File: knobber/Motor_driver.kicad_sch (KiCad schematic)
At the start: 28 parts, among them U601 TMC6300-LA-T, U602 LMV321

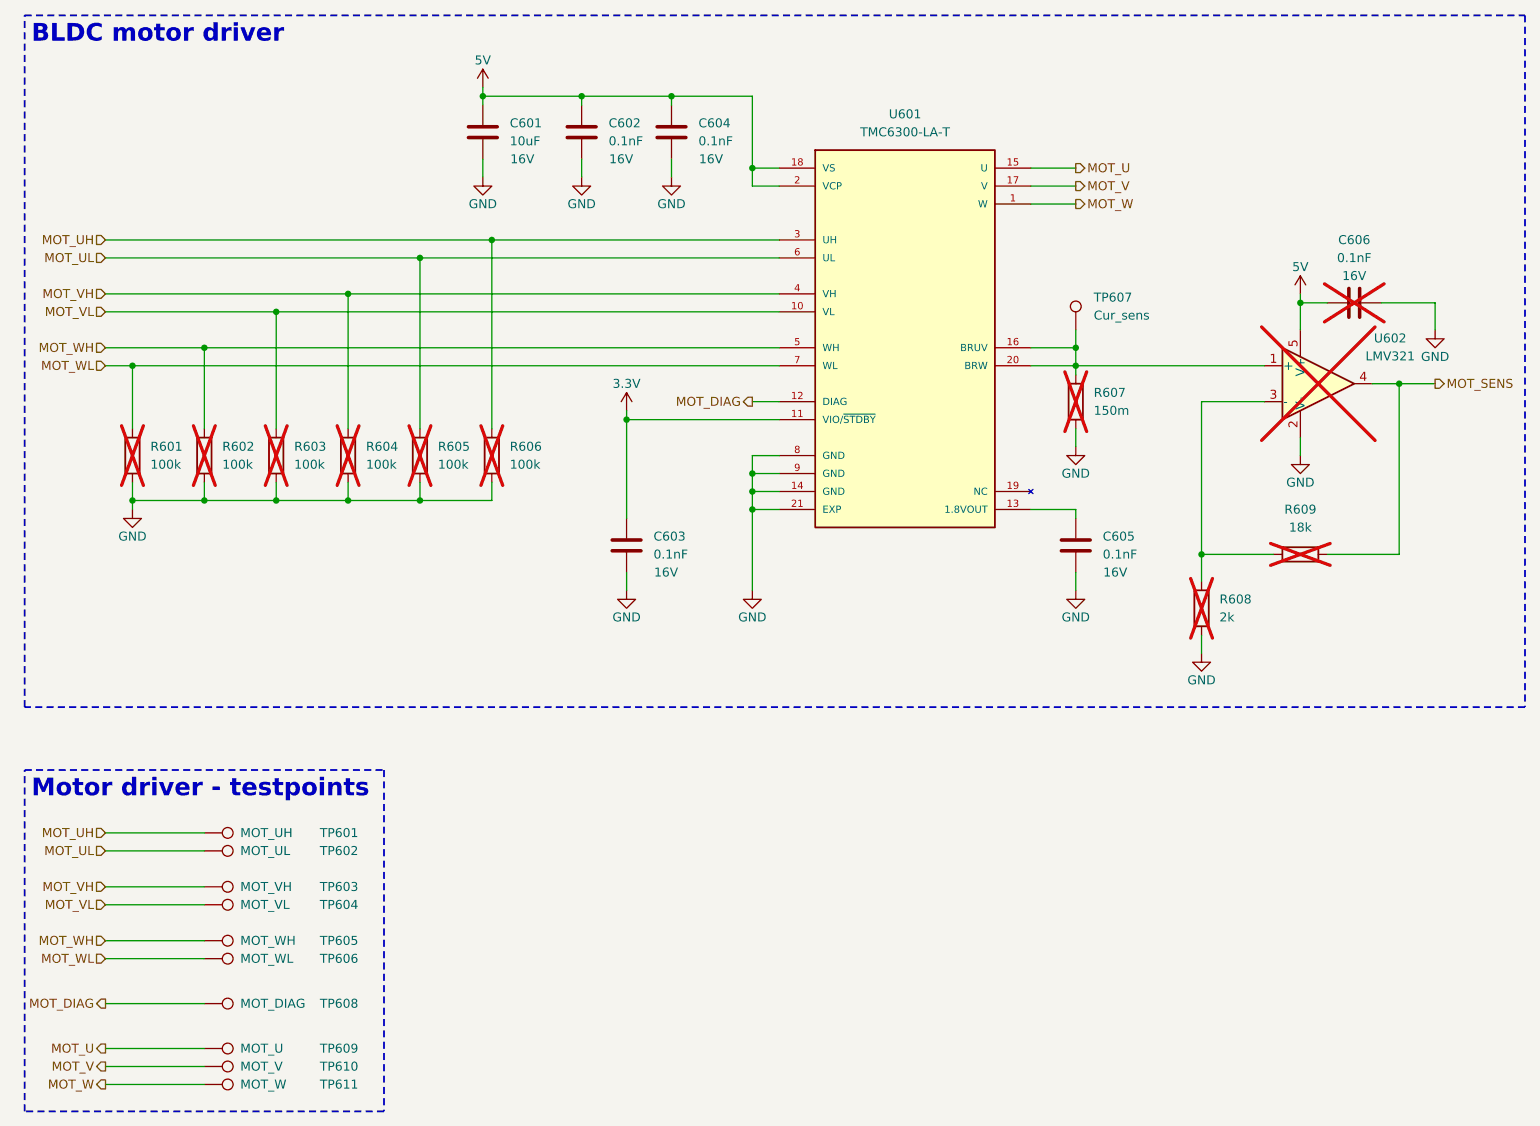
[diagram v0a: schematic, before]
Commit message: Updated schematic and PCB
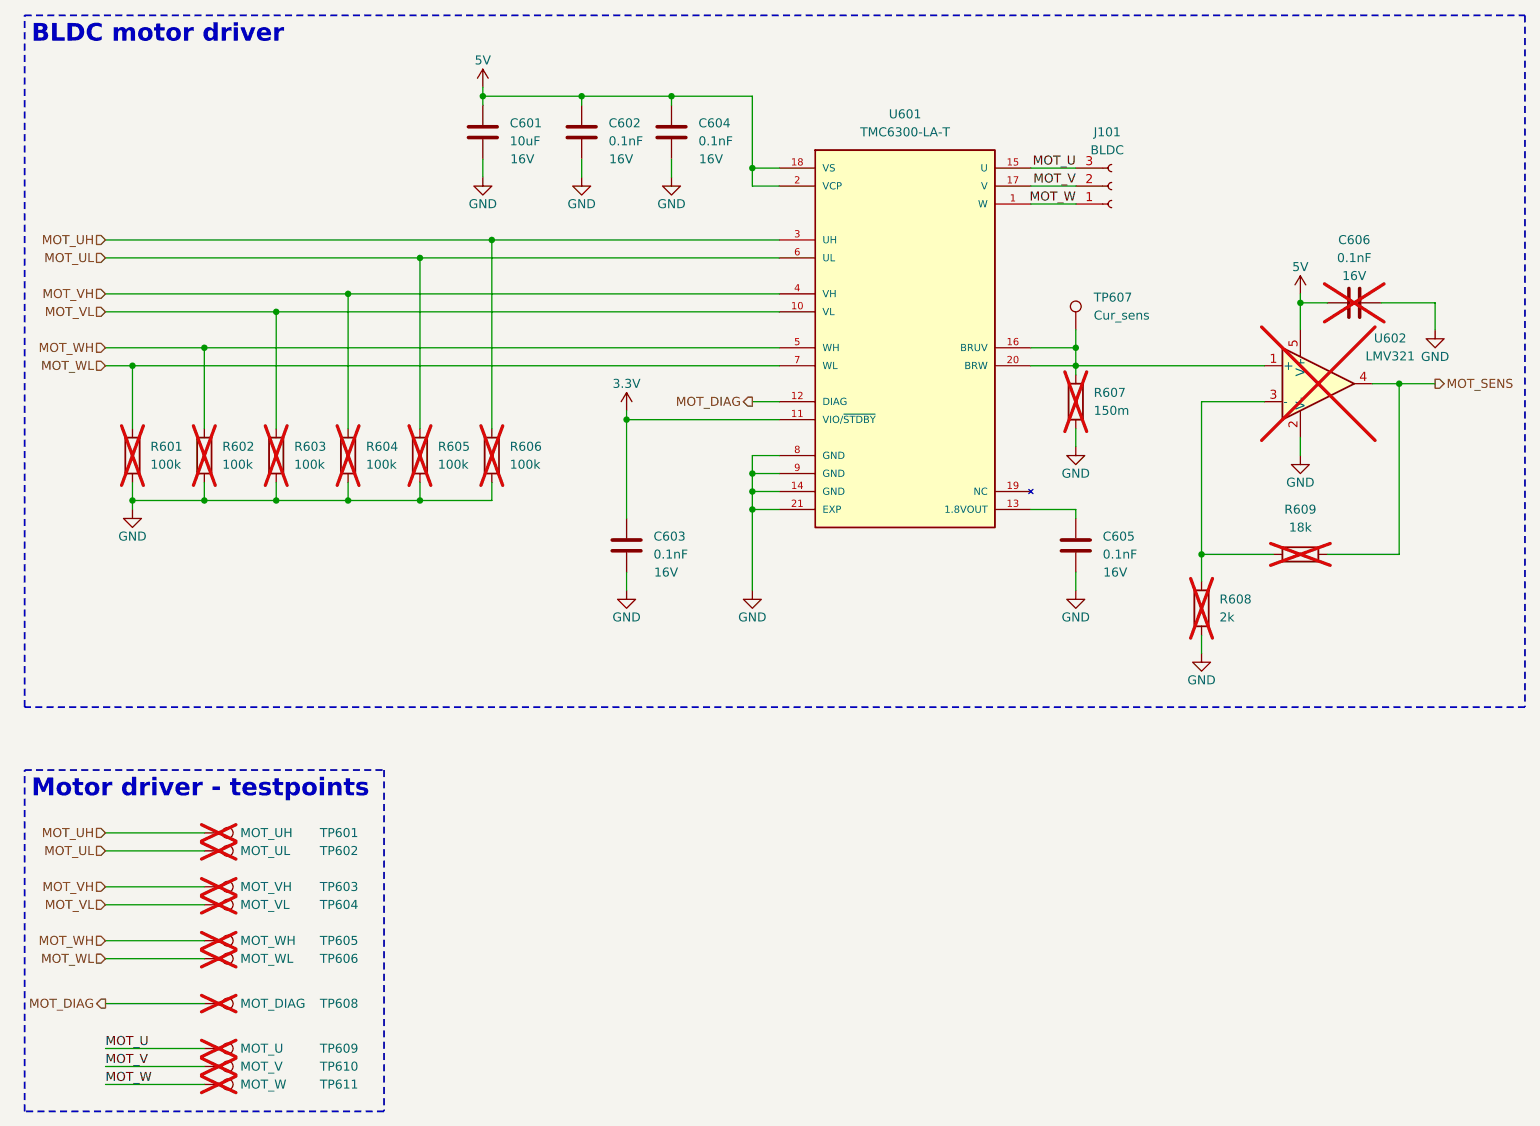
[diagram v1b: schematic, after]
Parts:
- added J101: BLDC, Connector_Molex:Molex_SPOX_5267-03A_1x03_P2.50mm_Vertical, symbol Connector:Conn_01x03_Socket
- TP601, TP602, TP603, TP604, TP605, TP606, TP608, TP609, TP610, TP611: now not fitted; now left out of the parts list
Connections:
- net MOT_U: now also J101.3 (Pin_3)
- net MOT_V: now also J101.2 (Pin_2)
- net MOT_W: now also J101.1 (Pin_1)
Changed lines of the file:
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@@
 		)
 	)
-	(hierarchical_label "MOT_DIAG"
-		(shape output)
-		(at 54.61 162.56 180)
+	(label "MOT_V"
+		(at 54.61 171.45 0)
 		(effects
 			(font
 				(size 1.27 1.27)
 			)
-			(justify right)
+			(justify left bottom)
 		)
 	)
-	(hierarchical_label "MOT_WL"
-		(shape input)
-		(at 54.61 156.21 180)
+	(label "MOT_W"
+		(at 54.61 173.99 0)
 		(effects
 			(font
 				(size 1.27 1.27)
 			)
-			(justify right)
+			(justify left bottom)
 		)
 	)
-	(hierarchical_label "MOT_WH"
-		(shape input)
-		(at 54.61 69.85 180)
+	(label "MOT_V"
+		(at 191.77 46.99 180)
 		(effects
 			(font
 				(size 1.27 1.27)
 			)
-			(justify right)
+			(justify right bottom)
 		)
 	)
-	(hierarchical_label "MOT_W"
-		(shape output)
-		(at 54.61 173.99 180)
+	(label "MOT_U"
+		(at 191.77 44.45 180)
 		(effects
 			(font
 				(size 1.27 1.27)
 			)
-			(justify right)
+			(justify right bottom)
 		)
 	)
-	(hierarchical_label "MOT_W"
-		(shape output)
-		(at 191.77 49.53 0)
+	(label "MOT_W"
+		(at 191.77 49.53 180)
 		(effects
 			(font
 				(size 1.27 1.27)
 			)
-			(justify left)
+			(justify right bottom)
 		)
 	)
-	(hierarchical_label "MOT_U"
-		(shape output)
-		(at 191.77 44.45 0)
+	(label "MOT_U"
+		(at 54.61 168.91 0)
 		(effects
 			(font
 				(size 1.27 1.27)
 			)
-			(justify left)
+			(justify left bottom)
 		)
 	)
-	(hierarchical_label "MOT_V"
+	(hierarchical_label "MOT_DIAG"
 		(shape output)
-		(at 191.77 46.99 0)
+		(at 54.61 162.56 180)
 		(effects
 			(font
 				(size 1.27 1.27)
 			)
-			(justify left)
+			(justify right)
 		)
 	)
-	(hierarchical_label "MOT_U"
-		(shape output)
-		(at 54.61 168.91 180)
+	(hierarchical_label "MOT_WL"
+		(shape input)
+		(at 54.61 156.21 180)
 		(effects
 			(font
@@
 	(hierarchical_label "MOT_WH"
 		(shape input)
-		(at 54.61 153.67 180)
+		(at 54.61 69.85 180)
 		(effects
 			(font
@@
 		)
 	)
-	(hierarchical_label "MOT_UL"
+	(hierarchical_label "MOT_WH"
 		(shape input)
-		(at 54.61 140.97 180)
+		(at 54.61 153.67 180)
 		(effects
 			(font
@@
 		)
 	)
-	(hierarchical_label "MOT_V"
-		(shape output)
-		(at 54.61 171.45 180)
+	(hierarchical_label "MOT_UL"
+		(shape input)
+		(at 54.61 140.97 180)
 		(effects
 			(font
@@
 		(unit 1)
 		(exclude_from_sim no)
-		(in_bom yes)
-		(on_board yes)
-		(dnp no)
+		(in_bom no)
+		(on_board no)
+		(dnp yes)
 		(property "Reference" "TP601"
 			(at 87.63 138.43 90)
@@
 	)
 	(symbol
-		(lib_id "Connector:TestPoint")
-		(at 68.58 146.05 270)
+		(lib_id "Connector:Conn_01x03_Socket")
+		(at 196.85 46.99 0)
 		(mirror x)
 		(unit 1)
@@
 		(on_board yes)
 		(dnp no)
+		(fields_autoplaced yes)
+		(property "Reference" "J101"
+			(at 196.215 39.37 0)
+			(effects
+				(font
+					(size 1.27 1.27)
+				)
+			)
+		)
+		(property "Value" "BLDC"
+			(at 196.215 41.91 0)
+			(effects
+				(font
+					(size 1.27 1.27)
+				)
+			)
+		)
+		(property "Footprint" "Connector_Molex:Molex_SPOX_5267-03A_1x03_P2.50mm_Vertical"
+			(at 196.85 46.99 0)
+			(effects
+				(font
+					(size 1.27 1.27)
+				)
+				(hide yes)
+			)
+		)
+		(property "Datasheet" "~"
+			(at 196.85 46.99 0)
+			(effects
+				(font
+					(size 1.27 1.27)
+				)
+				(hide yes)
+			)
+		)
+		(property "Description" "Generic connector, single row, 01x03, script generated"
+			(at 196.85 46.99 0)
+			(effects
+				(font
+					(size 1.27 1.27)
+				)
+				(hide yes)
+			)
+		)
+		(pin "2"
+		)
+		(pin "1"
+		)
+		(pin "3"
+		)
+		(instances
+			(project "knobber"
+				(path "/09c102b8-dfc1-4666-b1e2-d0c53b401993/09b435d4-5eb0-4cf9-81af-6c2df0af7c36"
+					(reference "J101")
+					(unit 1)
+				)
+			)
+		)
+	)
+	(symbol
+		(lib_id "Connector:TestPoint")
+		(at 68.58 146.05 270)
+		(mirror x)
+		(unit 1)
+		(exclude_from_sim no)
+		(in_bom no)
+		(on_board no)
+		(dnp yes)
 		(property "Reference" "TP603"
 			(at 87.63 146.05 90)
@@
 		(unit 1)
 		(exclude_from_sim no)
-		(in_bom yes)
-		(on_board yes)
-		(dnp no)
+		(in_bom no)
+		(on_board no)
+		(dnp yes)
 		(property "Reference" "TP608"
 			(at 87.63 162.56 90)
@@
 		(unit 1)
 		(exclude_from_sim no)
-		(in_bom yes)
-		(on_board yes)
-		(dnp no)
+		(in_bom no)
+		(on_board no)
+		(dnp yes)
 		(property "Reference" "TP609"
 			(at 87.63 168.91 90)
@@
 		(unit 1)
 		(exclude_from_sim no)
-		(in_bom yes)
-		(on_board yes)
-		(dnp no)
+		(in_bom no)
+		(on_board no)
+		(dnp yes)
 		(property "Reference" "TP604"
 			(at 87.63 148.59 90)
@@
 		(unit 1)
 		(exclude_from_sim no)
-		(in_bom yes)
-		(on_board yes)
-		(dnp no)
+		(in_bom no)
+		(on_board no)
+		(dnp yes)
 		(property "Reference" "TP605"
 			(at 87.63 153.67 90)
@@
 		(unit 1)
 		(exclude_from_sim no)
-		(in_bom yes)
-		(on_board yes)
-		(dnp no)
+		(in_bom no)
+		(on_board no)
+		(dnp yes)
 		(property "Reference" "TP610"
 			(at 87.63 171.45 90)
@@
 		(unit 1)
 		(exclude_from_sim no)
-		(in_bom yes)
-		(on_board yes)
-		(dnp no)
+		(in_bom no)
+		(on_board no)
+		(dnp yes)
 		(property "Reference" "TP606"
 			(at 87.63 156.21 90)
@@
 		(unit 1)
 		(exclude_from_sim no)
-		(in_bom yes)
-		(on_board yes)
-		(dnp no)
+		(in_bom no)
+		(on_board no)
+		(dnp yes)
 		(property "Reference" "TP611"
 			(at 87.63 173.99 90)
@@
 		(unit 1)
 		(exclude_from_sim no)
-		(in_bom yes)
-		(on_board yes)
-		(dnp no)
+		(in_bom no)
+		(on_board no)
+		(dnp yes)
 		(property "Reference" "TP602"
 			(at 87.63 140.97 90)
